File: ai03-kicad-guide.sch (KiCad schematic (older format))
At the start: 14 parts

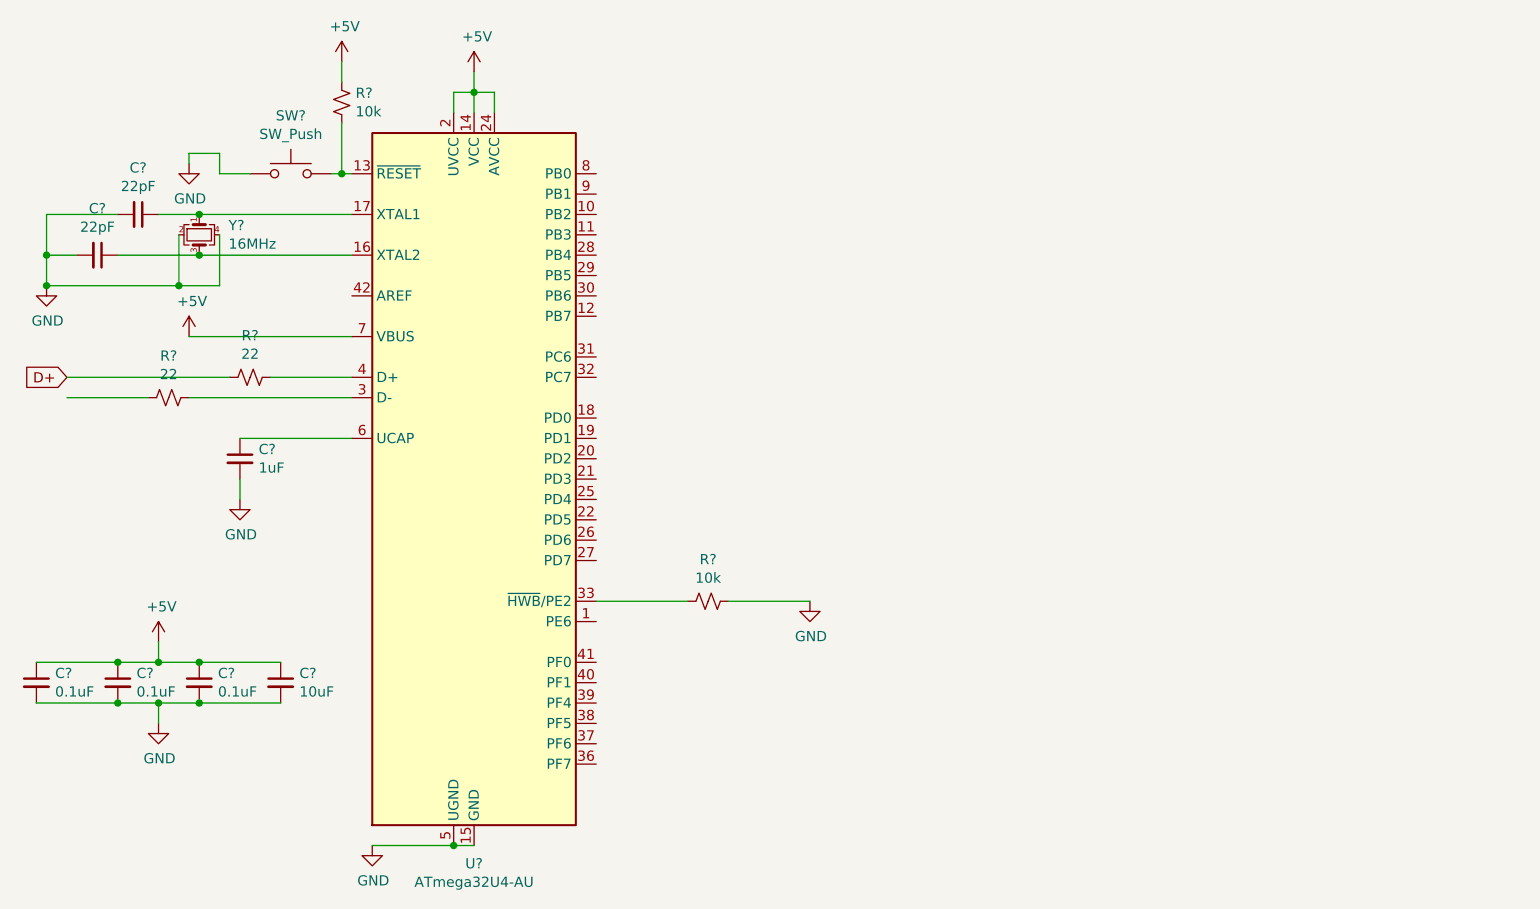
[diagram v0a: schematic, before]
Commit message: Added all component annotations and footprints
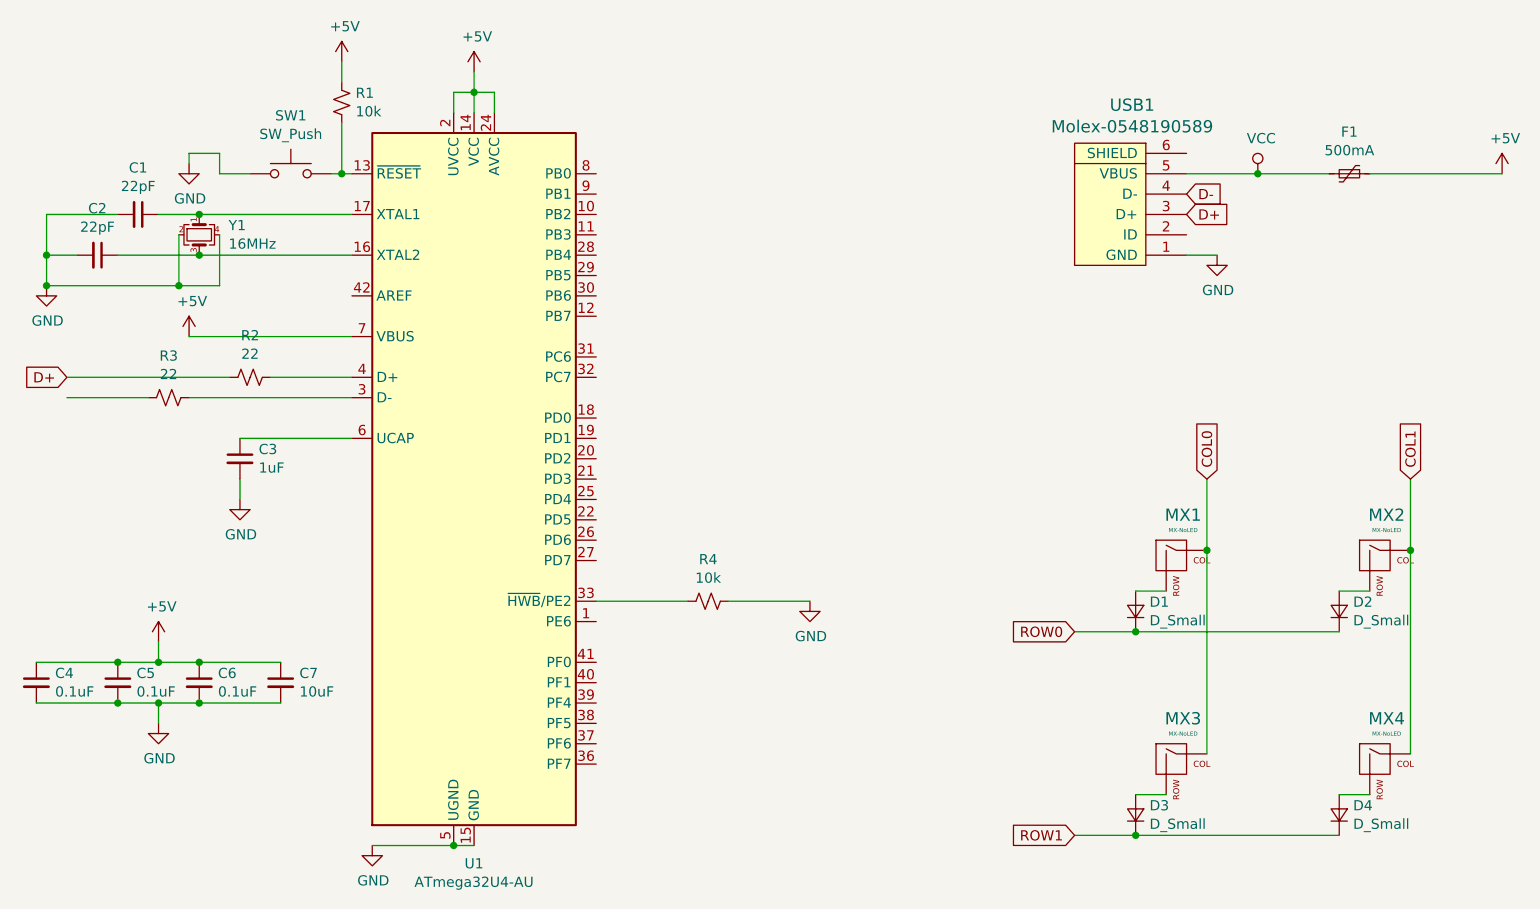
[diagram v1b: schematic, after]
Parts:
- added D1, D2, D3, D4: D_Small, Diode_SMD:D_0805_2012Metric, symbol Device:D_Small
- added F1: 500mA, Fuse:Fuse_0805_2012Metric, symbol Device:Polyfuse_Small
- added MX1, MX2, MX3: MX-NoLED, MX_Alps_Hybrid:MX-1U-NoLED, symbol MX_Alps_Hybrid:MX-NoLED
- added MX4: MX-NoLED, Resistor_SMD:R_0805_2012Metric, symbol MX_Alps_Hybrid:MX-NoLED
- added USB1: Molex-0548190589, random-keyboard-parts:Molex-0548190589, symbol random-keyboard-parts:Molex-0548190589
- C1, C2, C3, C4, C5, C6, C7: renamed from C?; footprint (none) -> Capacitor_SMD:C_0805_2012Metric
- R1, R2, R3, R4: renamed from R?; footprint (none) -> Resistor_SMD:R_0805_2012Metric
- SW1: renamed from SW?; footprint (none) -> random-keyboard-parts:SKQG-1155865
- Y1: renamed from Y?; footprint (none) -> Crystal:Crystal_SMD_3225-4Pin_3.2x2.5mm
- gave numbers to parts that had none: 1
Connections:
- net +5V: now also F1.1
- net D+: now also USB1.3 (D+)
- net GND: now also USB1.1 (GND)
- new net: D1.2 (A), MX1.2 (ROW)
- new net: D2.2 (A), MX2.2 (ROW)
- new net: D3.2 (A), MX3.2 (ROW)
- new net: D4.2 (A), MX4.2 (ROW)
- new net COL0: MX1.1 (COL), MX3.1 (COL)
- new net COL1: MX2.1 (COL), MX4.1 (COL)
- new net D-: USB1.4 (D-)
- new net ROW0: D1.1 (K), D2.1 (K)
- new net ROW1: D3.1 (K), D4.1 (K)
- new net VCC: F1.2, USB1.5 (VBUS)
